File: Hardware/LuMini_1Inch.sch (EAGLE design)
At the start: 25 parts, among them J1 DOUBLE_LED_PAD, J2 DOUBLE_LED_PAD, J3 DOUBLE_LED_PAD, J4 DOUBLE_LED_PAD

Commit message: Cleaning repo, changing name, pre review
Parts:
- removed J3: DOUBLE_LED_PAD, Andy:DOUBLE_LED_PAD
- added C1: 4.7uF, SparkFun-Capacitors:4.7UF-0603-6.3V-(10%)
- added H2, H3: STANDOFF_ELECTRICALSTANDOFF-ELECTRICAL-NOTHERMALS, SparkFun-Hardware:STANDOFF_ELECTRICALSTANDOFF-ELECTRICAL-NOTHERMALS
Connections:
- net 5V: now also C1.1; no longer J3.2
- net GND: now also C1.2, H2.P$1, H3.P$1; no longer J3.1
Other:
- note added: "Andy England"
- note added: "Decoupling Capacitor"
- note added: "Heat Sinking/Gronuding Standoffs"
- note added: "LED's"
- note added: "v03"
- moved on the sheet: D1, D10, D11, D12, D13, D14, D15, D16, D17, D18, D19, D2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

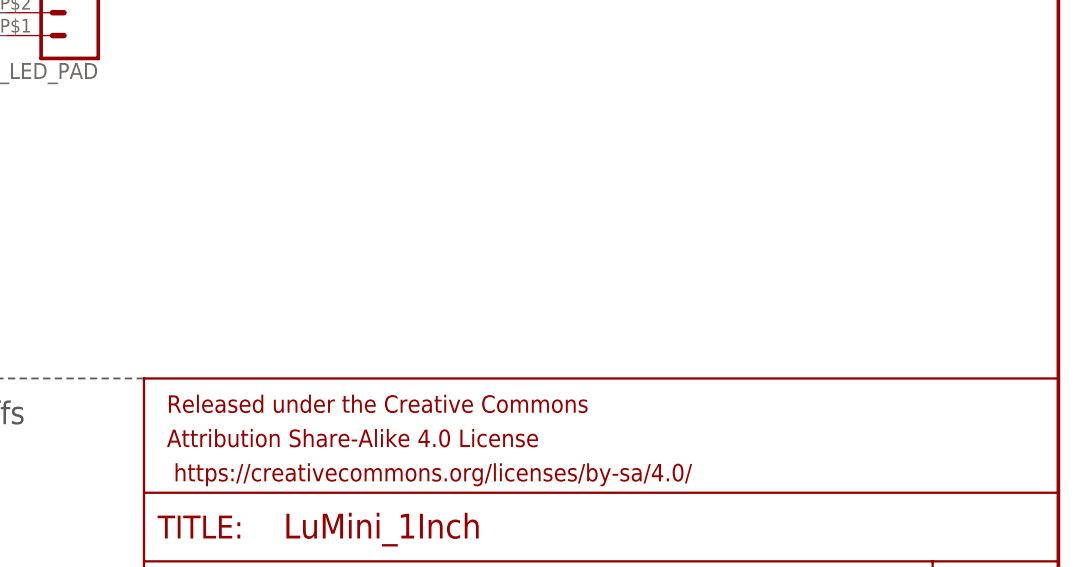
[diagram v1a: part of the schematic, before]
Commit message: adding silk
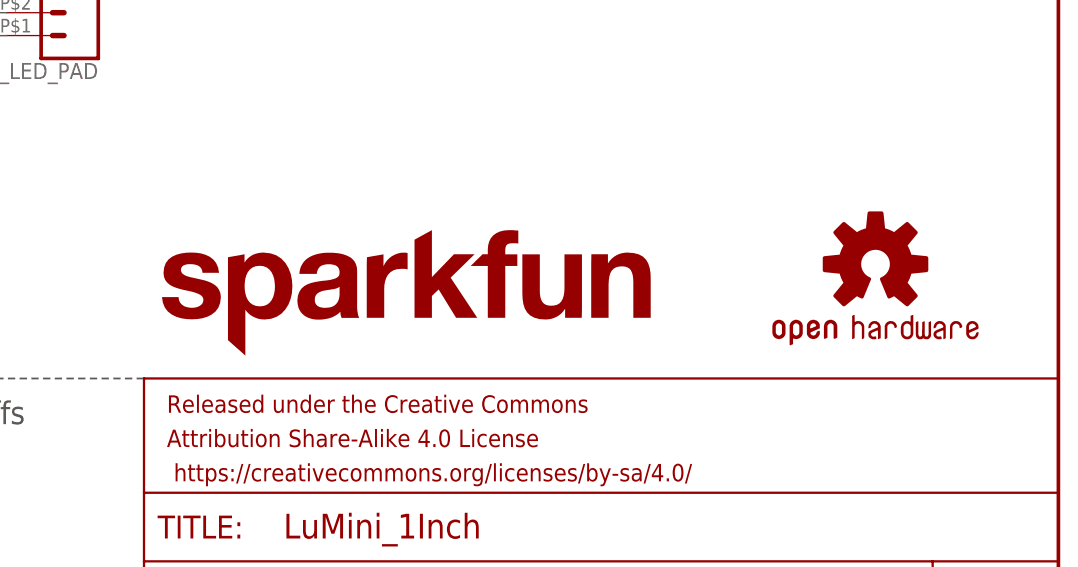
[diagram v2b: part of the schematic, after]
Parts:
- added LOGO1: SFE_LOGO_NAME.1_INCH, SparkFun-Aesthetics:SFE_LOGO_NAME.1_INCH
- added LOGO2: OSHW-LOGOS, SparkFun-Aesthetics:OSHW-LOGOS
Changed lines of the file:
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@@
 <part name="SUPPLY17" library="SparkFun-PowerSymbols" deviceset="5V" device=""/>
 <part name="GND22" library="SparkFun-PowerSymbols" deviceset="GND" device=""/>
+<part name="LOGO1" library="SparkFun-Aesthetics" deviceset="SFE_LOGO_NAME" device=".1_INCH"/>
+<part name="LOGO2" library="SparkFun-Aesthetics" deviceset="OSHW-LOGO" device="S"/>
 </parts>
 <sheets>
@@
 <instance part="SUPPLY17" gate="G$1" x="33.02" y="22.86"/>
 <instance part="GND22" gate="1" x="33.02" y="7.62"/>
+<instance part="LOGO1" gate="G$1" x="147.32" y="38.1"/>
+<instance part="LOGO2" gate="G$1" x="228.6" y="48.26"/>
 </instances>
 <busses>

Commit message: Post checklist
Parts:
- added FD1, FD2, FD3, FD4: FIDUCIALUFIDUCIAL, SparkFun-Aesthetics:FIDUCIALUFIDUCIAL
- added H1, H4: STANDOFF_ELECTRICALSTANDOFF-ELECTRICAL-NOTHERMALS, SparkFun-Hardware:STANDOFF_ELECTRICALSTANDOFF-ELECTRICAL-NOTHERMALS
- C1: value 4.7uF -> DNP
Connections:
- net GND: now also H1.P$1, H4.P$1
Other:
- note added: "Vin: 3.0V-5.5V"
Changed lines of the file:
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@@
 <part name="H3" library="SparkFun-Hardware" deviceset="STANDOFF_ELECTRICAL" device="STANDOFF-ELECTRICAL-NOTHERMALS"/>
 <part name="GND17" library="SparkFun-PowerSymbols" deviceset="GND" device=""/>
-<part name="C1" library="SparkFun-Capacitors" deviceset="4.7UF" device="-0603-6.3V-(10%)" value="4.7uF"/>
+<part name="C1" library="SparkFun-Capacitors" deviceset="4.7UF" device="-0603-6.3V-(10%)" value="DNP"/>
 <part name="SUPPLY17" library="SparkFun-PowerSymbols" deviceset="5V" device=""/>
 <part name="GND22" library="SparkFun-PowerSymbols" deviceset="GND" device=""/>
 <part name="LOGO1" library="SparkFun-Aesthetics" deviceset="SFE_LOGO_NAME" device=".1_INCH"/>
 <part name="LOGO2" library="SparkFun-Aesthetics" deviceset="OSHW-LOGO" device="S"/>
+<part name="H1" library="SparkFun-Hardware" deviceset="STANDOFF_ELECTRICAL" device="STANDOFF-ELECTRICAL-NOTHERMALS"/>
+<part name="H4" library="SparkFun-Hardware" deviceset="STANDOFF_ELECTRICAL" device="STANDOFF-ELECTRICAL-NOTHERMALS"/>
+<part name="FD1" library="SparkFun-Aesthetics" deviceset="FIDUCIAL" device="UFIDUCIAL"/>
+<part name="FD2" library="SparkFun-Aesthetics" deviceset="FIDUCIAL" device="UFIDUCIAL"/>
+<part name="FD3" library="SparkFun-Aesthetics" deviceset="FIDUCIAL" device="UFIDUCIAL"/>
+<part name="FD4" library="SparkFun-Aesthetics" deviceset="FIDUCIAL" device="UFIDUCIAL"/>
 </parts>
 <sheets>
@@
 <text x="17.272" y="30.48" size="2.54" layer="97" font="vector">Decoupling Capacitor</text>
 <text x="80.772" y="30.48" size="2.54" layer="97" font="vector">Heat Sinking/Gronuding Standoffs</text>
+<text x="122.428" y="135.636" size="2.54" layer="97" font="vector">Vin: 3.0V-5.5V</text>
 </plain>
 <instances>
@@
 <instance part="LOGO1" gate="G$1" x="147.32" y="38.1"/>
 <instance part="LOGO2" gate="G$1" x="228.6" y="48.26"/>
+<instance part="H1" gate="G$1" x="86.36" y="22.86"/>
+<instance part="H4" gate="G$1" x="86.36" y="10.16"/>
+<instance part="FD1" gate="G$1" x="228.6" y="20.32"/>
+<instance part="FD2" gate="G$1" x="231.14" y="20.32"/>
+<instance part="FD3" gate="G$1" x="233.68" y="20.32"/>
+<instance part="FD4" gate="G$1" x="236.22" y="20.32"/>
 </instances>
 <busses>
@@
 <pinref part="H2" gate="G$1" pin="P$1"/>
 <wire x1="96.52" y1="5.08" x2="96.52" y2="7.62" width="0.1524" layer="91"/>
-<wire x1="96.52" y1="7.62" x2="96.52" y2="22.86" width="0.1524" layer="91"/>
+<wire x1="96.52" y1="7.62" x2="96.52" y2="10.16" width="0.1524" layer="91"/>
+<wire x1="96.52" y1="10.16" x2="96.52" y2="22.86" width="0.1524" layer="91"/>
 <wire x1="96.52" y1="22.86" x2="99.06" y2="22.86" width="0.1524" layer="91"/>
 <pinref part="H3" gate="G$1" pin="P$1"/>
 <wire x1="99.06" y1="7.62" x2="96.52" y2="7.62" width="0.1524" layer="91"/>
 <junction x="96.52" y="7.62"/>
-</segment>
-<segment>
+<pinref part="H1" gate="G$1" pin="P$1"/>
+<wire x1="96.52" y1="22.86" x2="93.98" y2="22.86" width="0.1524" layer="91"/>
+<junction x="96.52" y="22.86"/>
+<pinref part="H4" gate="G$1" pin="P$1"/>
+<wire x1="93.98" y1="10.16" x2="96.52" y2="10.16" width="0.1524" layer="91"/>
+<junction x="96.52" y="10.16"/>
+</segment>
+<segment>

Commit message: qc checklist changes
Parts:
- D1, D10, D11, D12, D13, D14, D15, D16, D17, D18, D19, D2, D20, D3, D4, D5, D6, D7, D8, D9: value APA1022020 -> APA102-2020; device SparkFun-LED:APA1022020 -> SparkFun-LED:APA102-2020
- H1, H2, H3, H4: value STANDOFF_ELECTRICALSTANDOFF-ELECTRICAL-NOTHERMALS -> STANDOFF_ELECTRICAL-NOTHERMALS; device SparkFun-Hardware:STANDOFF_ELECTRICALSTANDOFF-ELECTRICAL-NOTHERMALS -> SparkFun-Hardware:STANDOFF_ELECTRICAL-NOTHERMALS
- J1, J2, J4: value DOUBLE_LED_PAD -> SOLDER_PAD_2; device Andy:DOUBLE_LED_PAD -> SparkFun-Connectors:SOLDER_PAD_2
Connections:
- net N$2 renamed CI
- net N$3 renamed DI
- net N$41 renamed CO
- net N$42 renamed DO
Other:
- note added: "Heat Sinking/Grounding Standoffs"
- note added: "Solder Pads"
- note removed: "Heat Sinking/Gronuding Standoffs"
- moved on the sheet: D1, D10, D11, D12, D13, D14, D15, D16, D17, D18, D19, D2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

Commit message: version number change
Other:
- note added: "v10"
- note removed: "v03"
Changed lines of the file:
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@@
 <plain>
 <text x="165.608" y="11.176" size="2.54" layer="94" font="vector">Andy England</text>
-<text x="236.474" y="6.604" size="2.54" layer="94" font="vector">v03</text>
+<text x="236.474" y="6.604" size="2.54" layer="94" font="vector">v10</text>
 <text x="122.428" y="163.576" size="2.54" layer="97" font="vector">LED's</text>
 <wire x1="147.32" y1="40.64" x2="66.04" y2="40.64" width="0.2032" layer="97" style="longdash"/>
